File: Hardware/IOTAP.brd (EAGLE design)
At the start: 120 x 110 mm, 48 parts, among them IC1 MCP9808-MSOP8, J1 POWER_JACK-SLOTS, J2 PoE, SW1 MODE

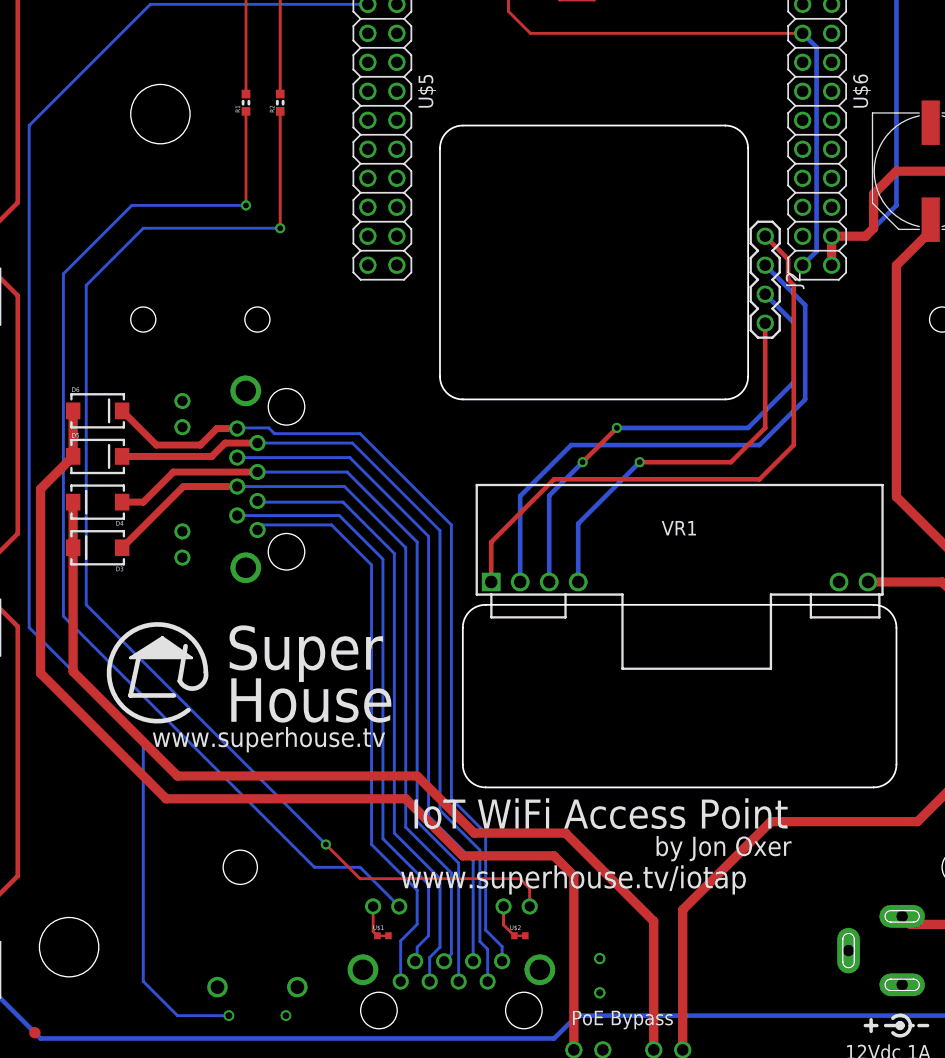
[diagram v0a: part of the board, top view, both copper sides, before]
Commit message: Fixed footprint for RJ45 socket.
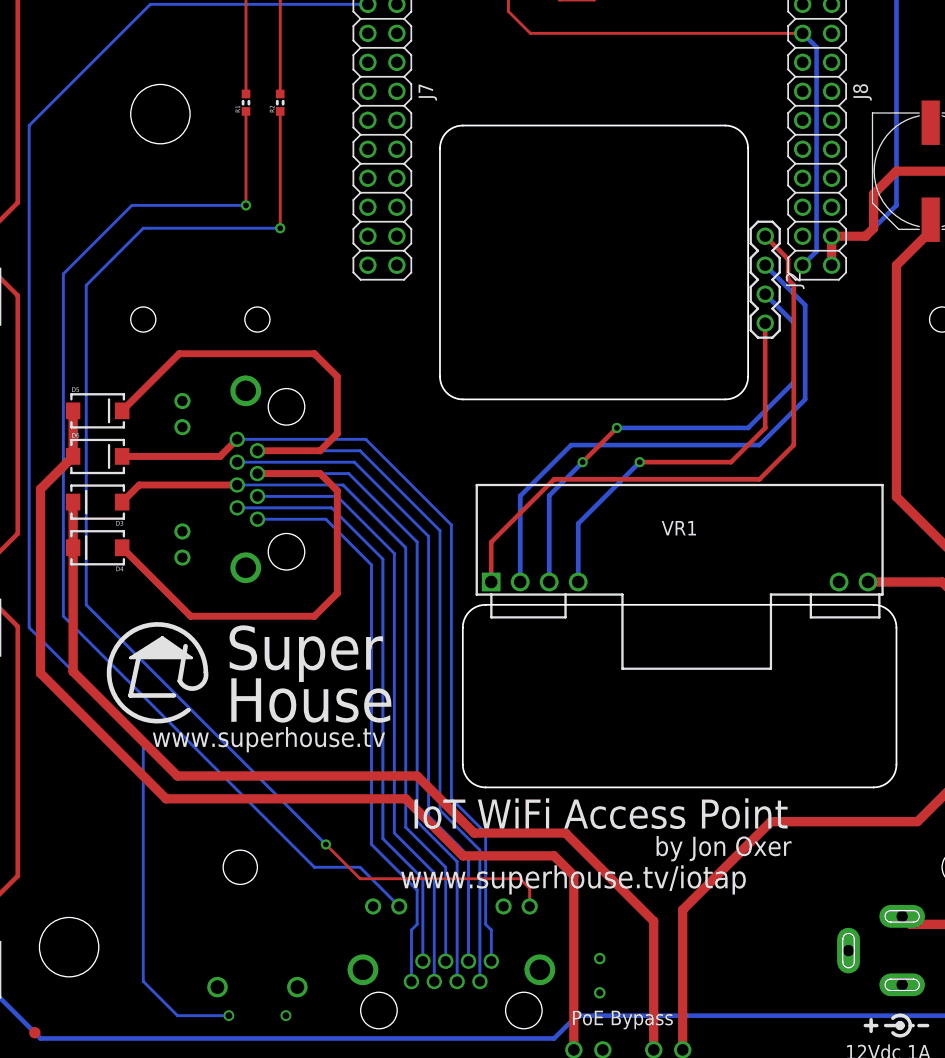
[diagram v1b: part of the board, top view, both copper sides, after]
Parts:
- removed U$1, U$2: SJC-0402, SuperHouse-Jumpers:0402SJC
- moved D3 4.00 mm to (-44.0, 50.0)
- moved D4 4.00 mm to (-44.0, 46.0)
- moved D5 4.00 mm to (-44.0, 58.0)
- moved D6 4.00 mm to (-44.0, 54.0)
- renumbered U$3 to J5, U$4 to J6, U$5 to J7, U$6 to J8
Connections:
- removed net N$21: J5.9, U$1.1
- removed net N$24: J5.11, U$2.1
- net GND: now also J5.11, J5.9; no longer U$1.2, U$2.2
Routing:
- net POE2+: track 69.5 -> 95.2 mm
- net POE1-: track 72.8 -> 94.2 mm
- net N$24: track 2.96 -> 0.00 mm
- net N$21: track 2.73 -> 0.00 mm
- net POE2-: track 74.3 -> 72.3 mm
- net POE1+: track 67.4 -> 65.4 mm
- net N$2: track 52.1 -> 51.3 mm

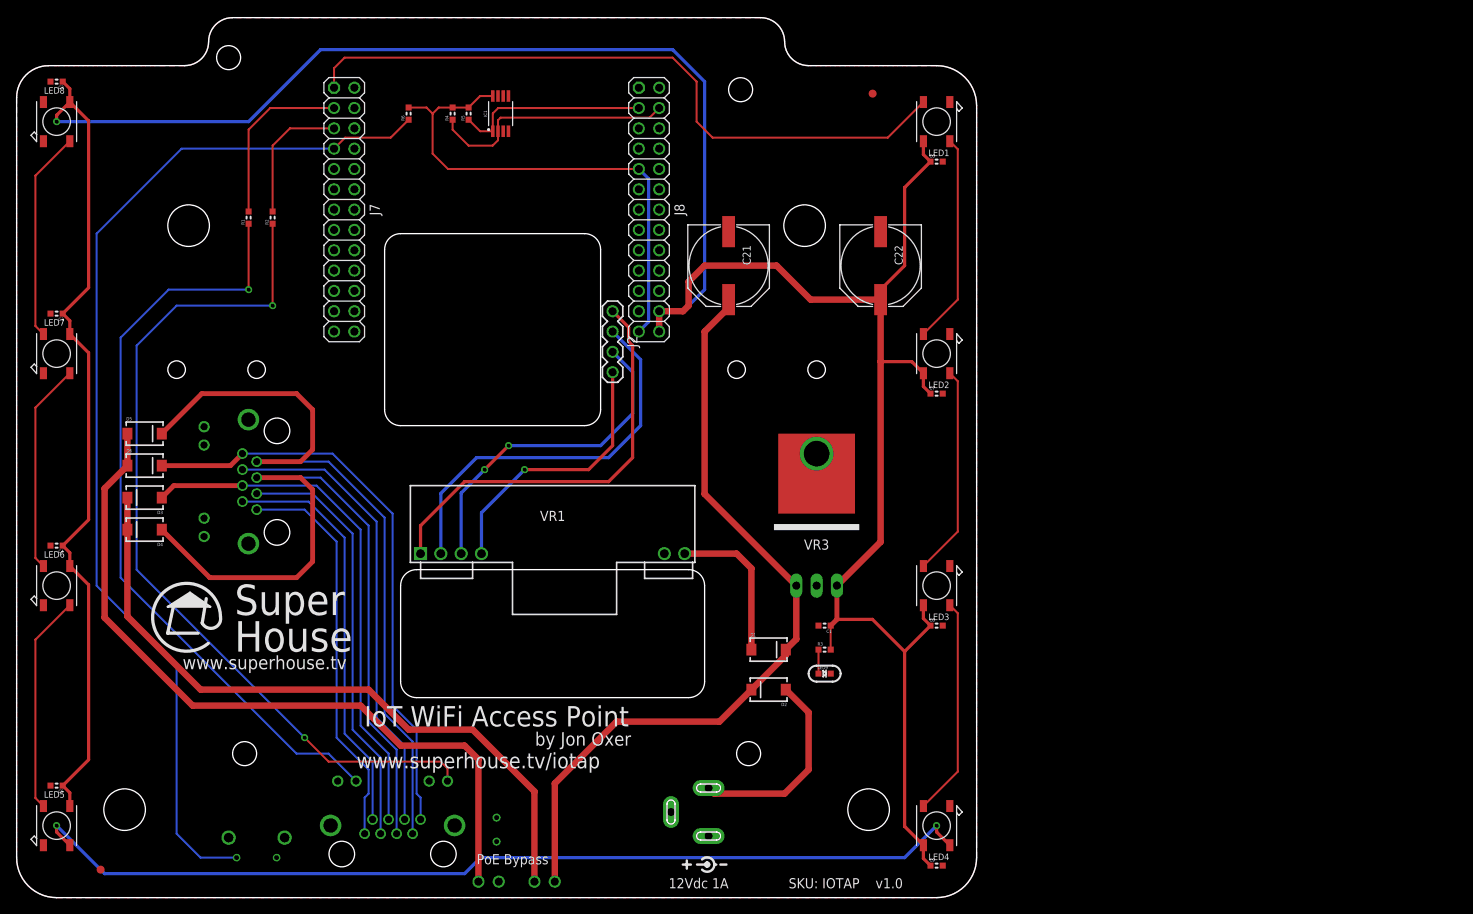
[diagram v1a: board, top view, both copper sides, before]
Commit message: Major redesign based on Raspberry Pi Zero 2.
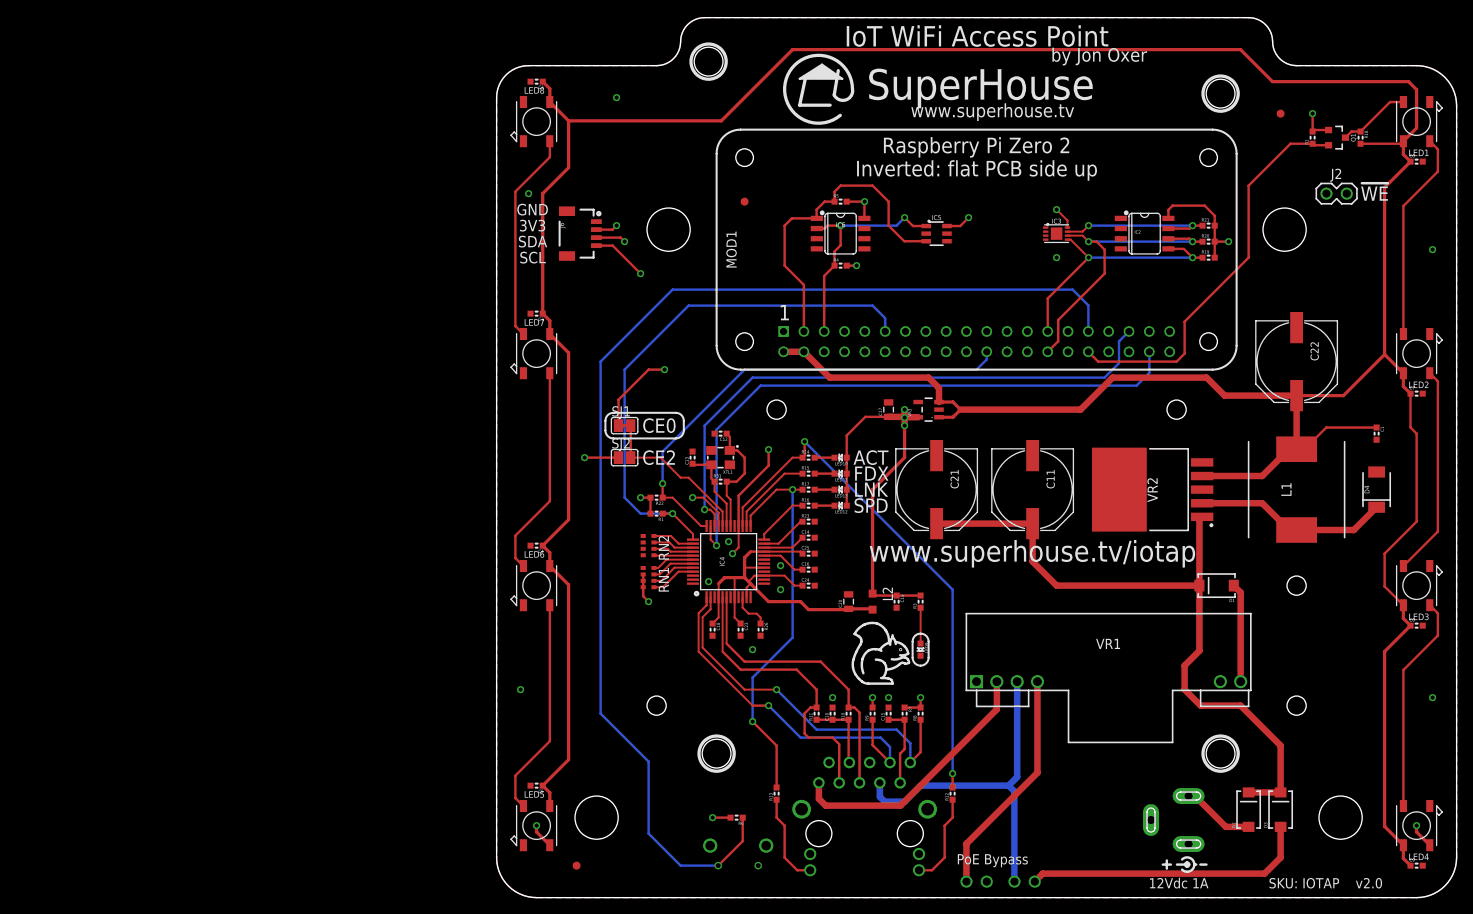
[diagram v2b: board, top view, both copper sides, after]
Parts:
- removed D5, D6: 1N4004, SuperHouse-Diodes:SMA-DIODE
- removed IC1: MCP9808-MSOP8, SuperHouse-Sensors:MSOP-8
- removed J7, J8: M02X13-S, SuperHouse-Connectors:2X13-S
- added C10, C14, C18: 10nF, SuperHouse-Capacitors:C0603
- added C11: 330uF 50V, SuperHouse-Capacitors:PANASONIC_G
- added C12, C13: 18pF, SuperHouse-Capacitors:C0603
- added C15: 22nF, SuperHouse-Capacitors:C0603
- added C16: 4.7uF, SuperHouse-Capacitors:C0603
- added C17, C20: 10uF, SuperHouse-Capacitors:C0805
- added C19, C23, C24, C25: 100nF, SuperHouse-Capacitors:C0603
- added FID3: FIDUCIAL1X2.5, SuperHouse-Symbols:FIDUCIAL-1X2.5
- added IC2: CAT24C32-SOIC8, SuperHouse-ICs:SOIC8
- added IC3: CAT24C32-UDFN8, SuperHouse-ICs:UDFN8
- added IC4: W5500-LQFP, SuperHouse-ICs:LQFP48
- added IC5: MCP24AA025E48-SOT23-6, SuperHouse-ICs:SOT23-6
- added IC6: AT30TSE752A-SOIC8, SuperHouse-Sensors:SOIC8
- added L1: SMDRI127-330MT, SuperHouse-Inductors:INDPM120120X800N
- added L2: 1uH 250mA 0805, rcl:L2012C
- added LED10, LED11, LED12: GREEN, SuperHouse-LEDs:LED-0603
- added LED13: YELLOW, SuperHouse-LEDs:LED-0603
- added MOD1: RASPI-ZERO-INV, SuperHouse-Modules:RPI-ZERO-INV
- added Q1: 2N7002, SuperHouse-Transistors:SOT23-3
- added R10, R11, R8, R9: 49R9 1%, SuperHouse-Resistors:R0603
- added R12, R13, R14, R15, R16, R17: 470R, SuperHouse-Resistors:R0603
- added R18, R22, R23: 10K, SuperHouse-Resistors:R0603
- added R19, R20: 4K7, SuperHouse-Resistors:R0603
- added R21: 1K, SuperHouse-Resistors:R0603
- added R26: 12.4K 1%, SuperHouse-Resistors:R0603
- added R31: 1M, SuperHouse-Resistors:R0603
- added R7: 10R, SuperHouse-Resistors:R0603
- added RN1, RN2: 10K, SuperHouse-Resistors:CAY16
- added SJ1: CE0, SuperHouse-Jumpers:SJC
- added SJ2: CE2, SuperHouse-Jumpers:SJ
- added VR2: LM2596S-5.0, SuperHouse-Regulators:TO170P1435X465-6N
- added XTL1: 25MHz, SuperHouse-Oscillators:CRYSTAL-SMD-3X2
- C21: value 330uF 25V -> 330uF 50V
- D1, D2, D3: value 1N4004 -> SS56
- D4: value 1N4004 -> PMEG3050EP,115; device SuperHouse-Diodes:SMA-DIODE -> SuperHouse-Diodes:SOD-128
- J2: value PoE -> !WRITE; device SuperHouse-Connectors:1X04-S -> SuperHouse-Connectors:1X02
- J5: value RJHSE538X-INVERTED -> ARJM11D7-114-AB-EW2; device SuperHouse-Connectors:RJHSE538X -> SuperHouse-Connectors:ARJM11D7114ABEW2
- J6: value RJHSE538X-INVERTED -> (none); device SuperHouse-Connectors:RJHSE538X -> SuperHouse-Connectors:1X04_QWIIC_1MM_RA
- LED9: value (none) -> BLUE
- R1, R2: value 220R -> 10K
- VR1: value DP1435-SIL -> DP1435-12V
- VR3: value L78S05CV -> AP2112KSOT25; device SuperHouse-Regulators:TO220 -> SuperHouse-Regulators:SOT23-5
- moved D4 154.1 mm to (110.0, 51.0), turned to 90 degrees
- moved D3 147.3 mm to (98.0, 11.0), turned to 90 degrees
- moved R2 130.4 mm to (102.0, 95.0)
- moved R6 97.1 mm to (30.0, 10.0), turned to 180 degrees
- moved J2 92.4 mm to (105.0, 88.0), turned to 0 degrees
- moved C1 73.1 mm to (110.0, 58.0), turned to 270 degrees
- moved VR1 71.3 mm to (76.5, 27.0)
- moved R1 63.0 mm to (20.0, 48.0), turned to 180 degrees
- moved D2 61.8 mm to (94.0, 11.0), turned to 90 degrees
- moved J4 61.0 mm to (60.0, 2.00)
- moved SW1 60.2 mm to (30.2, 4.00)
- moved J1 60.0 mm to (86.5, -1.00)
- moved C2 60.0 mm to (5.00, 102.0)
- moved C3 60.0 mm to (5.00, 73.0)
- moved C4 60.0 mm to (5.00, 44.0)
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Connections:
- removed net GPIO2_B5: J7.1, LED1.4-DIN
- removed net GPIO2_B6: J7.3, R1.2
- removed net GPIO2_B7: J7.5, R2.2
- removed net GPIO2_C0: J7.7, R6.1, SW1.P$1
- removed net N$6: J5.10, R1.1
- removed net N$7: D5.A, D6.A, J4.1
- removed net N$8: J5.12, R2.1
- removed net POE1+: D3.A, J5.4, J6.4
- removed net POE1-: D5.C, J5.7, J6.7
- removed net POE2+: D4.A, J5.5, J6.5
- removed net POE2-: D6.C, J5.8, J6.8
- removed net SCL0: IC1.2, J8.4, R4.1
- removed net SCL1: J8.21
- removed net SDA0: IC1.1, J8.3, R5.1
- removed net SDA1: J8.23
- new net !ETH_CS: IC4.32, SJ1.2, SJ2.2
- new net 1V2O: C14.1, IC4.22
- new net 3V3A: C18.1, C20.1, C23.1, C24.1, C25.1, IC4.11, IC4.15, IC4.17, IC4.21, IC4.4, IC4.8, L2.2
- new net ACTLED: IC4.27, R12.2, R14.1
- new net FDXLED: IC4.26, R15.1
- new net ID_SCL: IC2.6, IC3.6, MOD1.28, R20.1
- new net ID_SDA: IC2.5, IC3.5, MOD1.27, R19.1
- new net IO10_COPI: MOD1.19
- new net IO11_SCK: MOD1.23
- new net IO12_LEDS: MOD1.32, Q1.2, R2.1
- new net IO16_!CE2: MOD1.36, SJ2.1
- new net IO17_!ETH_RST: IC4.37, MOD1.11, R1.1
- new net IO18_!CE0: MOD1.12, SJ1.1
- new net IO19_CIPO1: IC4.34, MOD1.35
- new net IO20_COPI1: IC4.35, MOD1.38
- new net IO21_SCK1: IC4.33, MOD1.40
- new net IO25_!ETH_INT: IC4.36, MOD1.22, R22.1
- new net IO2_SDA: IC5.3, IC6.1, J6.3, MOD1.3, R5.1
- new net IO3_SCL: IC5.1, IC6.2, J6.4, MOD1.5, R4.1
- new net IO6_!BUTTON: MOD1.31, R6.1, SW1.P$1
- new net IO8: MOD1.24
- new net IO9_CIPO: MOD1.21
- new net LEDS: LED1.4-DIN, Q1.3, R18.1
- new net LINKLED: IC4.25, R13.2, R17.1
- new net N$18: C13.1, IC4.31, R31.1, XTL1.3
- new net N$20: C10.1, J5.4, R10.1, R11.1
- new net N$26: LED12.C, R16.2
- new net N$27: C12.1, IC4.30, R31.2, XTL1.1
- new net N$28: LED13.C, R17.2
- new net N$31: C16.1, IC4.20
- new net N$32: C15.1, J5.9, R7.2
- new net N$327: LED11.C, R15.2
- new net N$329: LED10.C, R14.2
- new net N$33: IC4.10, R26.1
- new net N$34: IC4.23, R23.1
- new net N$36: IC4.45, RN1.1
- new net N$37: IC4.44, RN1.2
- new net N$38: IC4.43, RN1.3
- new net N$39: IC4.42, RN1.4
- new net N$40: IC4.41, RN2.1
- new net N$41: IC4.40, RN2.2
- new net N$42: IC4.39, RN2.3
- new net N$43: IC4.38, RN2.4
- new net RXIN: IC4.5, J5.3, R11.2
- new net RXIP: IC4.6, J5.5, R10.2
- new net SPDLED: IC4.24, R16.1
- new net TXON: IC4.1, J5.8, R9.1
- new net TXOP: IC4.2, J5.10, R8.1
- net 12V: now also C11.+, D3.C, VR2.1; no longer J3.2, VR3.1
- net 3.3V: now also C17.1, C19.1, IC2.8, IC3.8, IC4.28, IC5.6, IC6.8, J5.L1, J5.L3, J6.2, L2.1, LED10.A, LED11.A, LED12.A, LED13.A, Q1.1, R1.2, R19.2, R2.2, R20.2, R21.2, R22.2, R3.2, R7.1, R8.2, R9.2, RN1.6, RN1.7, RN1.8, VR3.5; no longer IC1.8, J8.25, J8.9
- net 5V: now also L1.2, MOD1.2, MOD1.4, R18.2, VR2.4, VR3.1; no longer J8.24, J8.26, R3.2
- net GND: now also C10.2, C11.-, C12.2, C13.2, C14.2, C15.2, C16.2, C17.2, C18.2, C19.2, C20.2, C23.2, C24.2, C25.2, D4.2, IC2.1, IC2.2, IC2.3, IC2.4, IC3.1, IC3.2, IC3.3, IC3.4, IC3.PAD, IC4.14, IC4.16, IC4.19, IC4.29, IC4.3, IC4.48, IC4.9, IC5.2, IC5.4, IC5.5, IC6.4, IC6.5, IC6.6, IC6.7, J2.2, J5.MH1, J5.MH2, J6.1, MOD1.14, MOD1.20, MOD1.25, MOD1.30, MOD1.34, MOD1.39, MOD1.6, MOD1.9, R23.2, R26.2, RN1.5, RN2.5, RN2.6, RN2.7, RN2.8, VR2.3, VR2.5, VR2.6, XTL1.2, XTL1.4; no longer IC1.4, IC1.5, IC1.6, IC1.7, J5.11, J5.9, J5.GND@1, J5.GND@2, J6.GND@1, J6.GND@2, J7.2, J8.1, J8.14, J8.17, J8.22, J8.8, VR3.HEATSINK, VR3.TAB
- net N$1: now also D3.A, J3.2; no longer J5.1, J6.1
- net N$2: now also D4.1, L1.1, VR2.2; no longer J5.2, J6.2
- net N$3: now also J5.L4, R13.1; no longer J5.3, J6.3
- net N$4: now also J5.L2, R12.1; no longer J5.6, J6.6
- net N$5: now also IC2.7, IC3.7, J2.1, R21.1; no longer D3.C, D4.C, J3.1
- net VA1: now also J5.6; no longer J2.1
- net VA2: now also J5.1; no longer J2.2
- net VB1: now also J3.1, J5.7; no longer J2.3
- net VB2: now also J4.1, J5.2; no longer J2.4
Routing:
- net IO6_!BUTTON: track 0.00 -> 147.9 mm
- net GPIO2_C0: track 132.8 -> 0.00 mm
- net N$8: track 108.0 -> 0.00 mm, vias 2 -> 0
- net N$6: track 96.7 -> 0.00 mm, vias 1 -> 0
- net POE2+: track 95.2 -> 0.00 mm
- net POE1-: track 94.2 -> 0.00 mm
- net N$7: track 93.5 -> 0.00 mm
- net GPIO2_B5: track 85.6 -> 0.00 mm
- net IO16_!CE2: track 0.00 -> 79.0 mm, vias 0 -> 1
- net IO21_SCK1: track 0.00 -> 77.3 mm, vias 0 -> 1
- net IO20_COPI1: track 0.00 -> 76.9 mm, vias 0 -> 1
- net IO2_SDA: track 0.00 -> 75.4 mm, vias 0 -> 1
- net IO19_CIPO1: track 0.00 -> 73.0 mm, vias 0 -> 1
- net POE2-: track 72.3 -> 0.00 mm
- net IO17_!ETH_RST: track 0.00 -> 66.6 mm, vias 0 -> 1
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- added copper zone on layer 15, net 3.3V
- added copper zone on layer 2, net GND
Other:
- outline, holes or cut-outs redrawn
- board text added: "!WE"
- board text added: "(C) 2021-2022 SuperHouse Automation Pty Ltd Released under the TAPR Open Hardware License www.tapr.org/OHL"
- board text added: "1"
- board text added: "3V3"
- board text added: "ACT"
- board text added: "CE0"
- board text added: "CE2"
- board text added: "FDX"
- board text added: "GND"
- board text added: "LNK"
- board text added: "Raspberry Pi Zero 2 Inverted: flat PCB side up"
- board text added: "SCL"
- board text added: "SDA"
- board text added: "SKU: IOTAP v2.0"
- board text added: "SPD"
- board text added: "SuperHouse"
- board text removed: "(C) 2021 SuperHouse Automation Pty Ltd Released under the TAPR Open Hardware License www.tapr.org/OHL"
- board text removed: "SKU: IOTAP v1.0"
- board text removed: "Super House"
